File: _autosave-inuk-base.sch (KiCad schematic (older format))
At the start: 4 parts

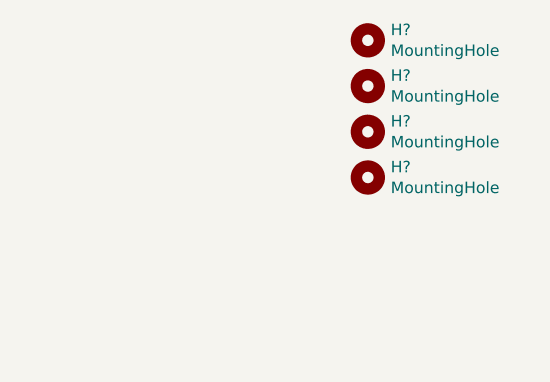
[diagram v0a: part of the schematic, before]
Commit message: added TP4056 module
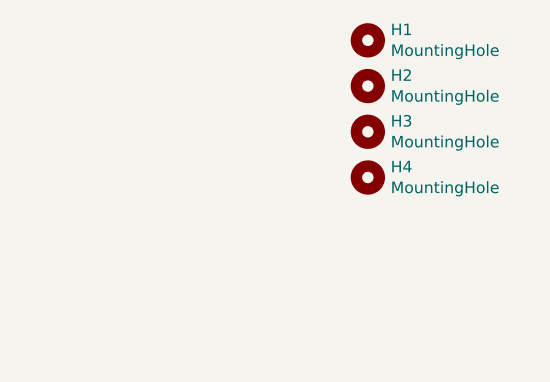
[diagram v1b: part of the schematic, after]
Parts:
- gave numbers to parts that had none: 4
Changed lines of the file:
@@
 	3900 2150 4400 2150
 $Comp
-L Mechanical:MountingHole H?
+L Mechanical:MountingHole H4
 U 1 1 5E7D5F82
 P 9550 1600
-F 0 "H?" H 9650 1646 50  0000 L CNN
+F 0 "H4" H 9650 1646 50  0000 L CNN
 F 1 "MountingHole" H 9650 1555 50  0000 L CNN
 F 2 "MountingHole:MountingHole_3.2mm_M3_Pad_Via" H 9650 1509 50  0001 L CNN
@@
 $EndComp
 $Comp
-L Mechanical:MountingHole H?
+L Mechanical:MountingHole H3
 U 1 1 5E7D615B
 P 9550 1400
-F 0 "H?" H 9650 1446 50  0000 L CNN
+F 0 "H3" H 9650 1446 50  0000 L CNN
 F 1 "MountingHole" H 9650 1355 50  0000 L CNN
 F 2 "MountingHole:MountingHole_3.2mm_M3_Pad_Via" H 9650 1309 50  0001 L CNN
@@
 $EndComp
 $Comp
-L Mechanical:MountingHole H?
+L Mechanical:MountingHole H2
 U 1 1 5E7D677D
 P 9550 1200
-F 0 "H?" H 9650 1246 50  0000 L CNN
+F 0 "H2" H 9650 1246 50  0000 L CNN
 F 1 "MountingHole" H 9650 1155 50  0000 L CNN
 F 2 "MountingHole:MountingHole_3.2mm_M3_Pad_Via" H 9650 1109 50  0001 L CNN
@@
 $EndComp
 $Comp
-L Mechanical:MountingHole H?
+L Mechanical:MountingHole H1
 U 1 1 5E7D6AF7
 P 9550 1000
-F 0 "H?" H 9650 1046 50  0000 L CNN
+F 0 "H1" H 9650 1046 50  0000 L CNN
 F 1 "MountingHole" H 9650 955 50  0000 L CNN
 F 2 "MountingHole:MountingHole_3.2mm_M3_Pad_Via" H 9650 909 50  0001 L CNN
